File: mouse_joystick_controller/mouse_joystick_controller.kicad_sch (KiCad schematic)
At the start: 0 parts

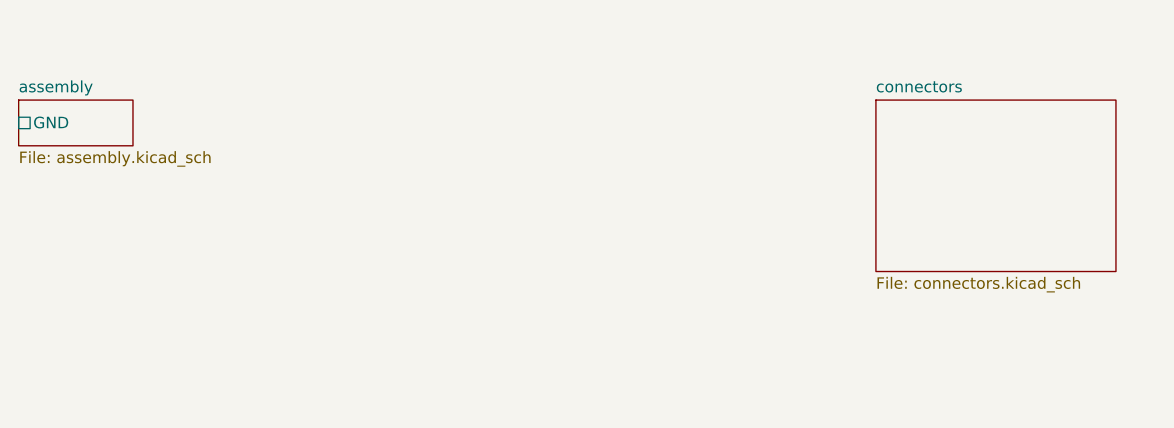
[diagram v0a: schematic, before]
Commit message: Add some driver components
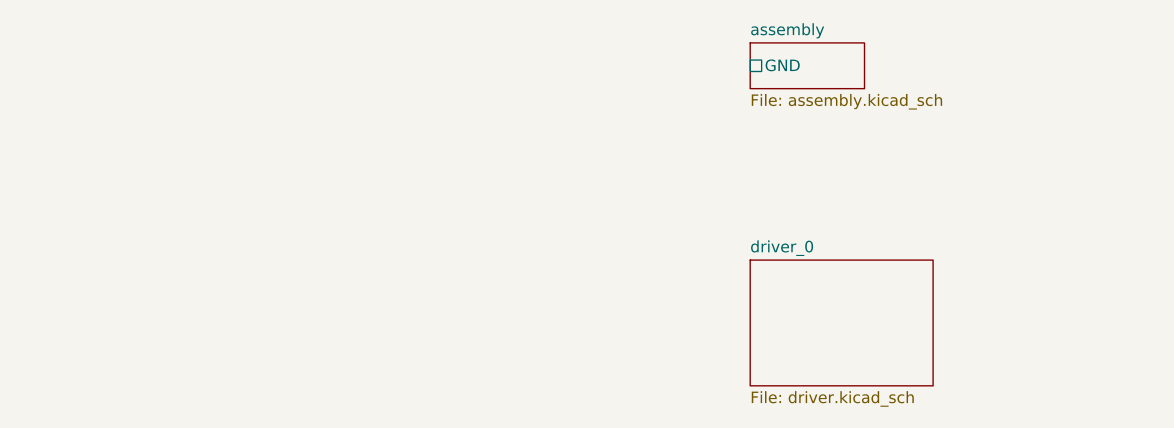
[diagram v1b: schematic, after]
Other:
- removed sheet connectors
- added sheet driver_0 (driver.kicad_sch)
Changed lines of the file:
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@@
     (company "Howard Hughes Medical Institute")
   )
-  (sheet (at 52.07 54.61) (size 12.7 5.08) (fields_autoplaced)
+  (sheet (at 133.35 72.39) (size 20.32 13.97) (fields_autoplaced)
     (stroke (width 0.1524) (type solid))
     (fill (color 0 0 0 0.0000))
-    (property "Sheetname" "assembly" (at 52.07 53.8984 0)
+    (property "Sheetname" "driver_0" (at 133.35 71.6784 0)
       (effects (font (size 1.27 1.27)) (justify left bottom))
     )
-    (property "Sheetfile" "assembly.kicad_sch" (at 52.07 60.2746 0)
+    (property "Sheetfile" "driver.kicad_sch" (at 133.35 86.9446 0)
       (effects (font (size 1.27 1.27)) (justify left top))
     )
-    (pin "GND" passive (at 52.07 57.15 180)
+    (instances
+      (project "mouse_joystick_controller"
+        (path "/cc457ebc-4af6-4663-b19f-8cb38f061cb4" (page "3"))
+      )
+    )
+  )
+  (sheet (at 133.35 48.26) (size 12.7 5.08) (fields_autoplaced)
+    (stroke (width 0.1524) (type solid))
+    (fill (color 0 0 0 0.0000))
+    (property "Sheetname" "assembly" (at 133.35 47.5484 0)
+      (effects (font (size 1.27 1.27)) (justify left bottom))
+    )
+    (property "Sheetfile" "assembly.kicad_sch" (at 133.35 53.9246 0)
+      (effects (font (size 1.27 1.27)) (justify left top))
+    )
+    (pin "GND" passive (at 133.35 50.8 180)
       (effects (font (size 1.27 1.27)) (justify left))
     )
@@
       )
     )
-  )
-  (sheet (at 147.32 54.61) (size 26.67 19.05) (fields_autoplaced)
-    (stroke (width 0.1524) (type solid))
-    (fill (color 0 0 0 0.0000))
-    (property "Sheetname" "connectors" (at 147.32 53.8984 0)
-      (effects (font (size 1.27 1.27)) (justify left bottom))
-    )
-    (property "Sheetfile" "connectors.kicad_sch" (at 147.32 74.2446 0)
-      (effects (font (size 1.27 1.27)) (justify left top))
-    )
-    (instances
-      (project "mouse_joystick_controller"
-        (path "/cc457ebc-4af6-4663-b19f-8cb38f061cb4" (page "3"))
-      )
-    )

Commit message: Add some sheets
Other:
- added sheet brake (brake.kicad_sch)
- added sheet power (power.kicad_sch)
- sheet driver_0 ports: added +24V, +3.3V, DIR, GND, POWER_ENABLE, REF, REFR, STEP, UART_RX, UART_TX, UART_TX_ENABLE, ~{DRIVER_ENABLE}; removed none
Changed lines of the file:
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@@
   (title_block
     (title "mouse_joystick_controller")
-    (date "2023-04-04")
+    (date "2023-05-17")
     (rev "2.0")
     (company "Howard Hughes Medical Institute")
   )
-  (sheet (at 133.35 72.39) (size 20.32 13.97) (fields_autoplaced)
+  (wire (pts (xy 133.35 86.36) (xy 130.81 86.36))
+    (stroke (width 0) (type default))
+  )
+  (wire (pts (xy 161.29 66.04) (xy 163.83 66.04))
+    (stroke (width 0) (type default))
+  )
+  (wire (pts (xy 133.35 68.58) (xy 130.81 68.58))
+    (stroke (width 0) (type default))
+  )
+  (wire (pts (xy 133.35 83.82) (xy 130.81 83.82))
+    (stroke (width 0) (type default))
+  )
+  (wire (pts (xy 133.35 81.28) (xy 130.81 81.28))
+    (stroke (width 0) (type default))
+  )
+  (wire (pts (xy 133.35 66.04) (xy 130.81 66.04))
+    (stroke (width 0) (type default))
+  )
+  (wire (pts (xy 161.29 71.12) (xy 163.83 71.12))
+    (stroke (width 0) (type default))
+  )
+  (wire (pts (xy 133.35 88.9) (xy 130.81 88.9))
+    (stroke (width 0) (type default))
+  )
+  (wire (pts (xy 133.35 76.2) (xy 130.81 76.2))
+    (stroke (width 0) (type default))
+  )
+  (wire (pts (xy 133.35 50.8) (xy 130.81 50.8))
+    (stroke (width 0) (type default))
+  )
+  (wire (pts (xy 133.35 71.12) (xy 130.81 71.12))
+    (stroke (width 0) (type default))
+  )
+  (wire (pts (xy 133.35 78.74) (xy 130.81 78.74))
+    (stroke (width 0) (type default))
+  )
+  (wire (pts (xy 161.29 68.58) (xy 163.83 68.58))
+    (stroke (width 0) (type default))
+  )
+  (label "GND" (at 130.81 71.12 180) (fields_autoplaced)
+    (effects (font (size 1.27 1.27)) (justify right bottom))
+  )
+  (label "DIR_0" (at 130.81 78.74 180) (fields_autoplaced)
+    (effects (font (size 1.27 1.27)) (justify right bottom))
+  )
+  (label "UART_RX_0" (at 163.83 66.04 0) (fields_autoplaced)
+    (effects (font (size 1.27 1.27)) (justify left bottom))
+  )
+  (label "REF_0" (at 163.83 68.58 0) (fields_autoplaced)
+    (effects (font (size 1.27 1.27)) (justify left bottom))
+  )
+  (label "GND" (at 130.81 50.8 180) (fields_autoplaced)
+    (effects (font (size 1.27 1.27)) (justify right bottom))
+  )
+  (label "~{DRIVER_ENABLE_0}" (at 130.81 86.36 180) (fields_autoplaced)
+    (effects (font (size 1.27 1.27)) (justify right bottom))
+  )
+  (label "STEP_0" (at 130.81 76.2 180) (fields_autoplaced)
+    (effects (font (size 1.27 1.27)) (justify right bottom))
+  )
+  (label "POWER_ENABLE_0" (at 130.81 88.9 180) (fields_autoplaced)
+    (effects (font (size 1.27 1.27)) (justify right bottom))
+  )
+  (label "UART_TX_ENABLE_0" (at 130.81 81.28 180) (fields_autoplaced)
+    (effects (font (size 1.27 1.27)) (justify right bottom))
+  )
+  (label "REFR_0" (at 163.83 71.12 0) (fields_autoplaced)
+    (effects (font (size 1.27 1.27)) (justify left bottom))
+  )
+  (label "UART_TX_0" (at 130.81 83.82 180) (fields_autoplaced)
+    (effects (font (size 1.27 1.27)) (justify right bottom))
+  )
+  (label "+24V" (at 130.81 66.04 180) (fields_autoplaced)
+    (effects (font (size 1.27 1.27)) (justify right bottom))
+  )
+  (label "+3.3V" (at 130.81 68.58 180) (fields_autoplaced)
+    (effects (font (size 1.27 1.27)) (justify right bottom))
+  )
+  (sheet (at 182.88 57.15) (size 22.86 17.78) (fields_autoplaced)
     (stroke (width 0.1524) (type solid))
     (fill (color 0 0 0 0.0000))
-    (property "Sheetname" "driver_0" (at 133.35 71.6784 0)
+    (property "Sheetname" "brake" (at 182.88 56.4384 0)
       (effects (font (size 1.27 1.27)) (justify left bottom))
     )
-    (property "Sheetfile" "driver.kicad_sch" (at 133.35 86.9446 0)
+    (property "Sheetfile" "brake.kicad_sch" (at 182.88 75.5146 0)
       (effects (font (size 1.27 1.27)) (justify left top))
+    )
+    (instances
+      (project "mouse_joystick_controller"
+        (path "/cc457ebc-4af6-4663-b19f-8cb38f061cb4" (page "4"))
+      )
+    )
+  )
+  (sheet (at 133.35 63.5) (size 27.94 27.94) (fields_autoplaced)
+    (stroke (width 0.1524) (type solid))
+    (fill (color 0 0 0 0.0000))
+    (property "Sheetname" "driver_0" (at 133.35 62.7884 0)
+      (effects (font (size 1.27 1.27)) (justify left bottom))
+    )
+    (property "Sheetfile" "driver.kicad_sch" (at 133.35 92.0246 0)
+      (effects (font (size 1.27 1.27)) (justify left top))
+    )
+    (pin "POWER_ENABLE" input (at 133.35 88.9 180)
+      (effects (font (size 1.27 1.27)) (justify left))
+    )
+    (pin "~{DRIVER_ENABLE}" input (at 133.35 86.36 180)
+      (effects (font (size 1.27 1.27)) (justify left))
+    )
+    (pin "REFR" output (at 161.29 71.12 0)
+      (effects (font (size 1.27 1.27)) (justify right))
+    )
+    (pin "REF" output (at 161.29 68.58 0)
+      (effects (font (size 1.27 1.27)) (justify right))
+    )
+    (pin "UART_RX" output (at 161.29 66.04 0)
+      (effects (font (size 1.27 1.27)) (justify right))
+    )
+    (pin "UART_TX" input (at 133.35 83.82 180)
+      (effects (font (size 1.27 1.27)) (justify left))
+    )
+    (pin "UART_TX_ENABLE" input (at 133.35 81.28 180)
+      (effects (font (size 1.27 1.27)) (justify left))
+    )
+    (pin "GND" passive (at 133.35 71.12 180)
+      (effects (font (size 1.27 1.27)) (justify left))
+    )
+    (pin "STEP" input (at 133.35 76.2 180)
+      (effects (font (size 1.27 1.27)) (justify left))
+    )
+    (pin "DIR" input (at 133.35 78.74 180)
+      (effects (font (size 1.27 1.27)) (justify left))
+    )
+    (pin "+3.3V" passive (at 133.35 68.58 180)
+      (effects (font (size 1.27 1.27)) (justify left))
+    )
+    (pin "+24V" passive (at 133.35 66.04 180)
+      (effects (font (size 1.27 1.27)) (justify left))
     )
     (instances
@@
       )
     )
+  )
+  (sheet (at 173.99 29.21) (size 24.13 10.16) (fields_autoplaced)
+    (stroke (width 0.1524) (type solid))
+    (fill (color 0 0 0 0.0000))
+    (property "Sheetname" "power" (at 173.99 28.4984 0)
+      (effects (font (size 1.27 1.27)) (justify left bottom))
+    )
+    (property "Sheetfile" "power.kicad_sch" (at 173.99 39.9546 0)
+      (effects (font (size 1.27 1.27)) (justify left top))
+    )
+    (instances
+      (project "mouse_joystick_controller"
+        (path "/cc457ebc-4af6-4663-b19f-8cb38f061cb4" (page "5"))
+      )
+    )

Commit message: Modify brake
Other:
- sheet power ports: added +24V, +3.3V, GND; removed none

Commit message: Add some sheets
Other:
- added sheet audio (audio.kicad_sch)
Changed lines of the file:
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@@
     (effects (font (size 1.27 1.27)) (justify right bottom))
+  )
+  (sheet (at 217.17 57.15) (size 17.78 19.05) (fields_autoplaced)
+    (stroke (width 0.1524) (type solid))
+    (fill (color 0 0 0 0.0000))
+    (property "Sheetname" "audio" (at 217.17 56.4384 0)
+      (effects (font (size 1.27 1.27)) (justify left bottom))
+    )
+    (property "Sheetfile" "audio.kicad_sch" (at 217.17 76.7846 0)
+      (effects (font (size 1.27 1.27)) (justify left top))
+    )
+    (instances
+      (project "mouse_joystick_controller"
+        (path "/cc457ebc-4af6-4663-b19f-8cb38f061cb4" (page "6"))
+      )
+    )
   )
   (sheet (at 182.88 57.15) (size 22.86 17.78) (fields_autoplaced)

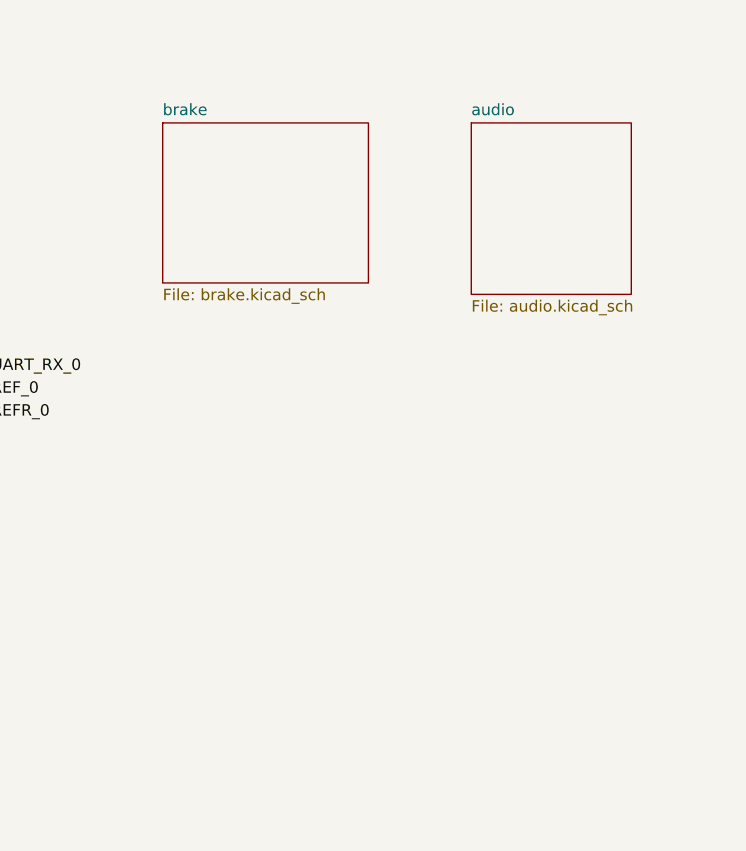
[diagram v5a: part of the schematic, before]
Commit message: Add encoder, lickport, and torque_sensor sheets
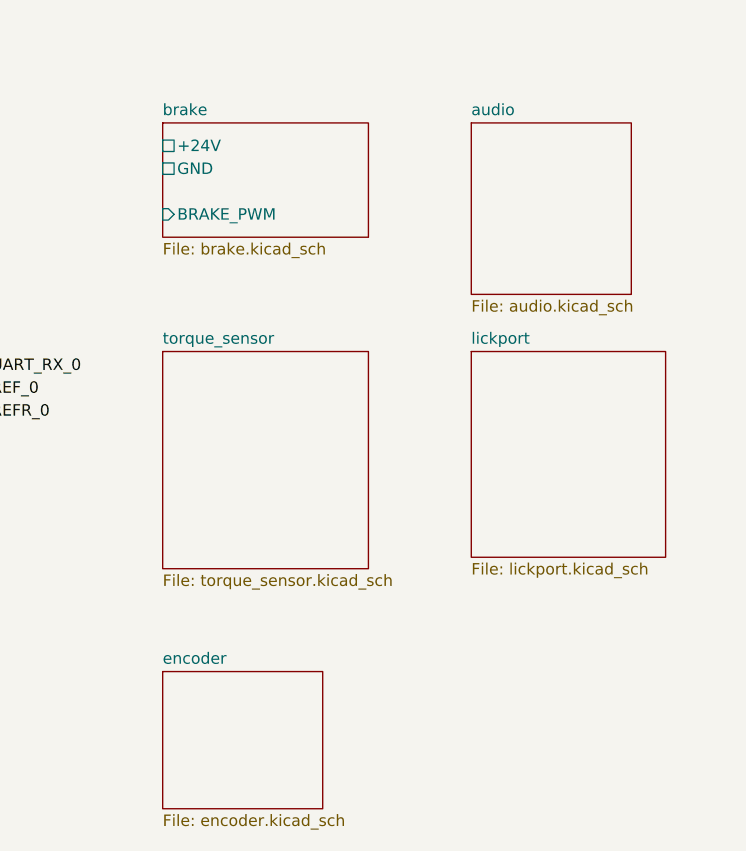
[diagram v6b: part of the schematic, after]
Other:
- added sheet encoder (encoder.kicad_sch)
- added sheet lickport (lickport.kicad_sch)
- added sheet torque_sensor (torque_sensor.kicad_sch)
- sheet brake ports: added +24V, BRAKE_PWM, GND; removed none
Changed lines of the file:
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@@
   (title_block
     (title "mouse_joystick_controller")
-    (date "2023-05-18")
+    (date "2023-05-22")
     (rev "2.0")
     (company "Howard Hughes Medical Institute")
@@
     )
   )
-  (sheet (at 182.88 57.15) (size 22.86 17.78) (fields_autoplaced)
+  (sheet (at 217.17 82.55) (size 21.59 22.86) (fields_autoplaced)
+    (stroke (width 0.1524) (type solid))
+    (fill (color 0 0 0 0.0000))
+    (property "Sheetname" "lickport" (at 217.17 81.8384 0)
+      (effects (font (size 1.27 1.27)) (justify left bottom))
+    )
+    (property "Sheetfile" "lickport.kicad_sch" (at 217.17 105.9946 0)
+      (effects (font (size 1.27 1.27)) (justify left top))
+    )
+    (instances
+      (project "mouse_joystick_controller"
+        (path "/cc457ebc-4af6-4663-b19f-8cb38f061cb4" (page "9"))
+      )
+    )
+  )
+  (sheet (at 182.88 57.15) (size 22.86 12.7) (fields_autoplaced)
     (stroke (width 0.1524) (type solid))
     (fill (color 0 0 0 0.0000))
@@
       (effects (font (size 1.27 1.27)) (justify left bottom))
     )
-    (property "Sheetfile" "brake.kicad_sch" (at 182.88 75.5146 0)
-      (effects (font (size 1.27 1.27)) (justify left top))
+    (property "Sheetfile" "brake.kicad_sch" (at 182.88 70.4346 0)
+      (effects (font (size 1.27 1.27)) (justify left top))
+    )
+    (pin "GND" passive (at 182.88 62.23 180)
+      (effects (font (size 1.27 1.27)) (justify left))
+    )
+    (pin "+24V" passive (at 182.88 59.69 180)
+      (effects (font (size 1.27 1.27)) (justify left))
+    )
+    (pin "BRAKE_PWM" input (at 182.88 67.31 180)
+      (effects (font (size 1.27 1.27)) (justify left))
     )
     (instances
@@
       )
     )
+  )
+  (sheet (at 182.88 82.55) (size 22.86 24.13) (fields_autoplaced)
+    (stroke (width 0.1524) (type solid))
+    (fill (color 0 0 0 0.0000))
+    (property "Sheetname" "torque_sensor" (at 182.88 81.8384 0)
+      (effects (font (size 1.27 1.27)) (justify left bottom))
+    )
+    (property "Sheetfile" "torque_sensor.kicad_sch" (at 182.88 107.2646 0)
+      (effects (font (size 1.27 1.27)) (justify left top))
+    )
+    (instances
+      (project "mouse_joystick_controller"
+        (path "/cc457ebc-4af6-4663-b19f-8cb38f061cb4" (page "7"))
+      )
+    )
+  )
+  (sheet (at 182.88 118.11) (size 17.78 15.24) (fields_autoplaced)
+    (stroke (width 0.1524) (type solid))
+    (fill (color 0 0 0 0.0000))
+    (property "Sheetname" "encoder" (at 182.88 117.3984 0)
+      (effects (font (size 1.27 1.27)) (justify left bottom))
+    )
+    (property "Sheetfile" "encoder.kicad_sch" (at 182.88 133.9346 0)
+      (effects (font (size 1.27 1.27)) (justify left top))
+    )
+    (instances
+      (project "mouse_joystick_controller"
+        (path "/cc457ebc-4af6-4663-b19f-8cb38f061cb4" (page "8"))
+      )
+    )
